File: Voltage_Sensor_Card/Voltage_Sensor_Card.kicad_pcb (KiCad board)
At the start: 2 copper layers, 59 parts, among them J1 Conn_01x04, U1 ACPL-C79B, U2 MEJ1S1205SC, U3 OPA2197xD

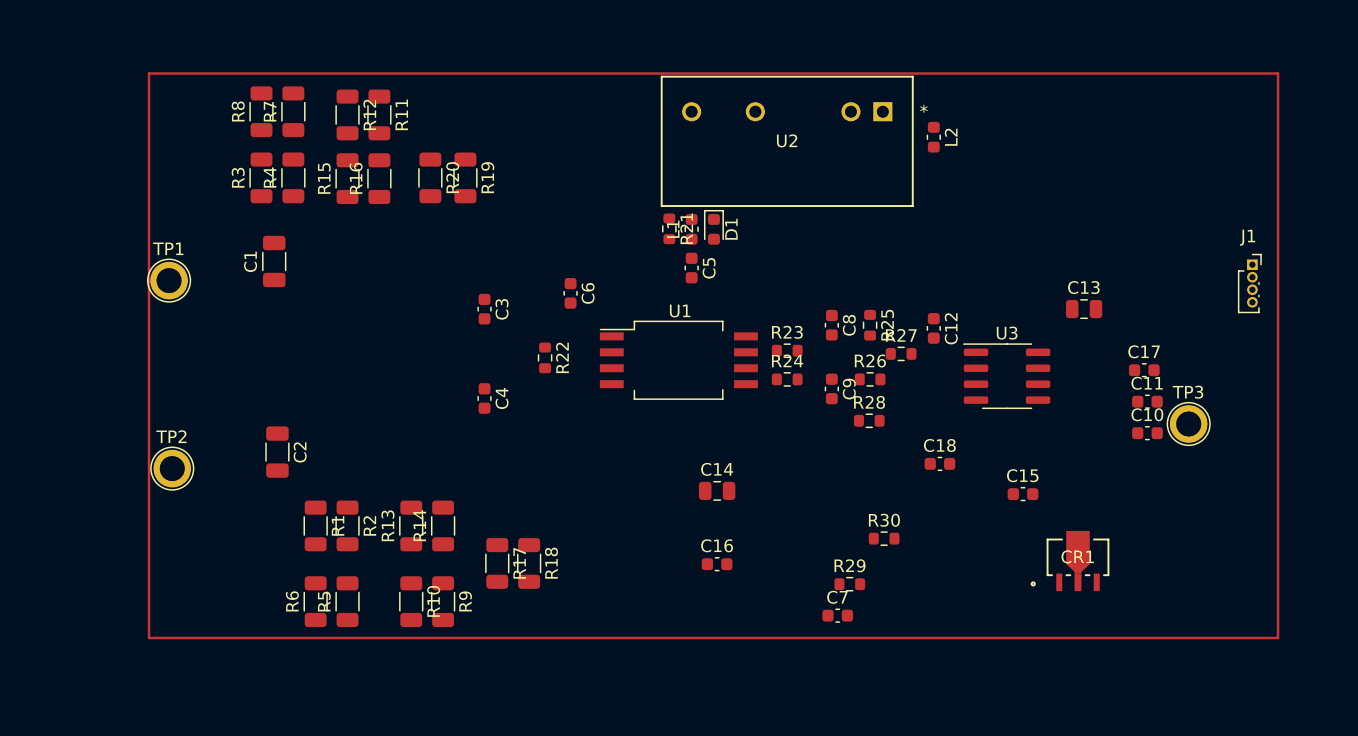
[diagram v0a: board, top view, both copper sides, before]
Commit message: Edited the layout.
Layout is not finalized yet, needs to be revised with an experienced team member.
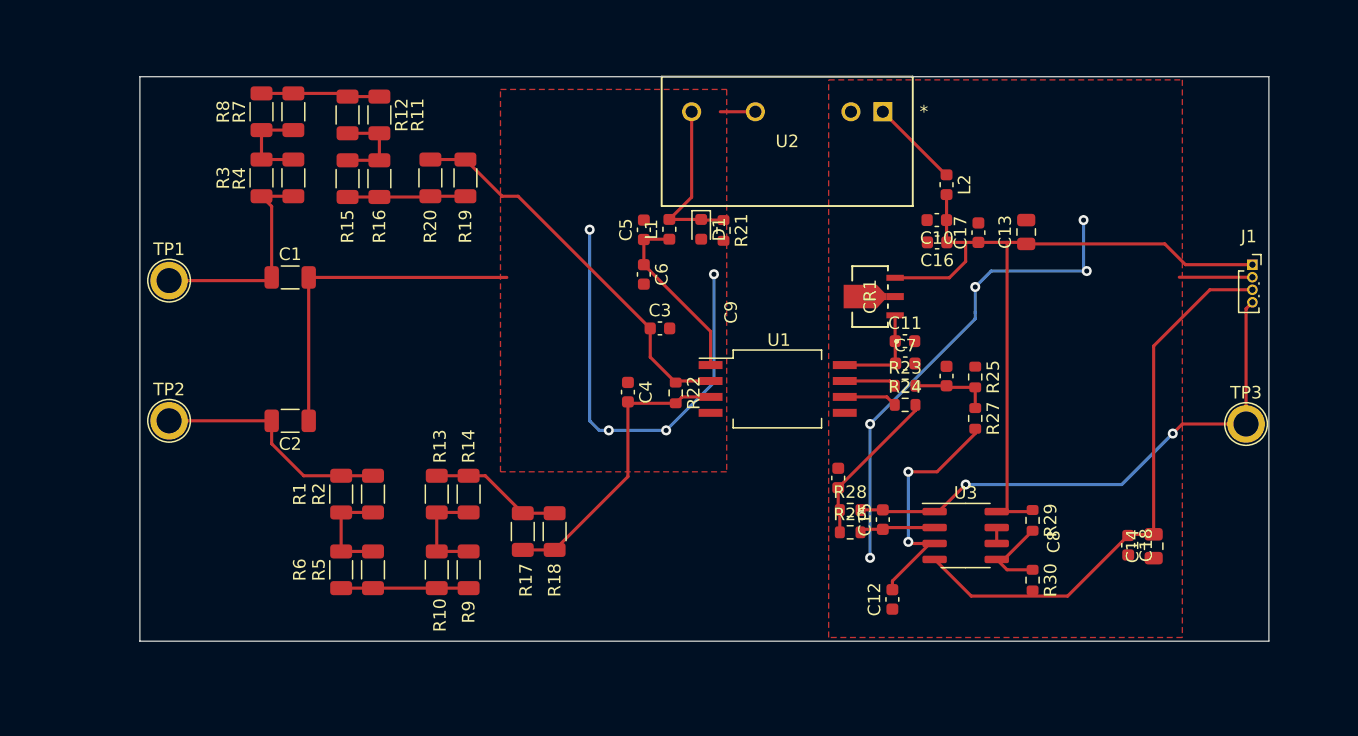
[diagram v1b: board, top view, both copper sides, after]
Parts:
- moved C14 35.1 mm to (180.1, 93.6), turned to 90 degrees
- moved C16 31.1 mm to (162.8, 69.3), turned to 180 degrees
- moved CR1 26.6 mm to (157.5, 73.7), turned to 90 degrees
- moved C10 23.9 mm to (162.8, 67.6), turned to 180 degrees
- moved C12 21.9 mm to (159.3, 97.8), turned to 90 degrees
- moved C7 20.8 mm to (160.3, 79.0)
- moved C11 19.9 mm to (160.3, 77.2)
- moved C17 17.2 mm to (166.1, 68.6), turned to 90 degrees
- moved C18 16.3 mm to (178.1, 93.5), turned to -90 degrees
- moved R29 15.4 mm to (170.4, 91.5), turned to -90 degrees
- moved C3 14.1 mm to (140.7, 76.2), turned to 0 degrees
- moved U3 13.1 mm to (165.1, 92.7)
- moved R26 12.3 mm to (155.9, 92.5)
- moved R30 12.3 mm to (170.4, 96.3), turned to -90 degrees
- moved C4 11.4 mm to (138.2, 81.3)
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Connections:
- C11 pad 1: +5V -> +5VA
- C5 pad 2: GND2 -> GND1
- CR1 pad 1: +5V -> +5VA
- D1 pad 2: GND2 -> GND1
- R21 pad 2: GND2 -> GND1
- U2 pad 5: GND2 -> GND1
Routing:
- net GND1: track 0.00 -> 65.7 mm, vias 0 -> 4
- net +15V: track 0.00 -> 60.9 mm
- net -15V: track 0.00 -> 45.5 mm
- net GND2: track 0.00 -> 44.5 mm, vias 0 -> 5
- net /Measure: track 0.00 -> 43.6 mm, vias 0 -> 2
- net Net-(C3-Pad1): track 0.00 -> 31.1 mm
- net Net-(C4-Pad2): track 0.00 -> 23.6 mm
- net Net-(C12-Pad2): track 0.00 -> 20.0 mm, vias 0 -> 2
- net Net-(C2-Pad2): track 0.00 -> 19.1 mm
- net Net-(C1-Pad1): track 0.00 -> 17.8 mm
- net +5V: track 0.00 -> 14.3 mm
- net Net-(D1-Pad1): track 0.00 -> 13.7 mm
- net Net-(C9-Pad1): track 0.00 -> 12.8 mm
- net Net-(R13-Pad2): track 0.00 -> 10.6 mm
- net Net-(R10-Pad1): track 0.00 -> 10.2 mm
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- added copper zone on F.Cu, net GND1
- added copper zone on F.Cu, net GND2
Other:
- board outline added: 90 x 45 mm

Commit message: Revized the layout.
Changed the orientation and placement of components, added all tracks and copper pours.
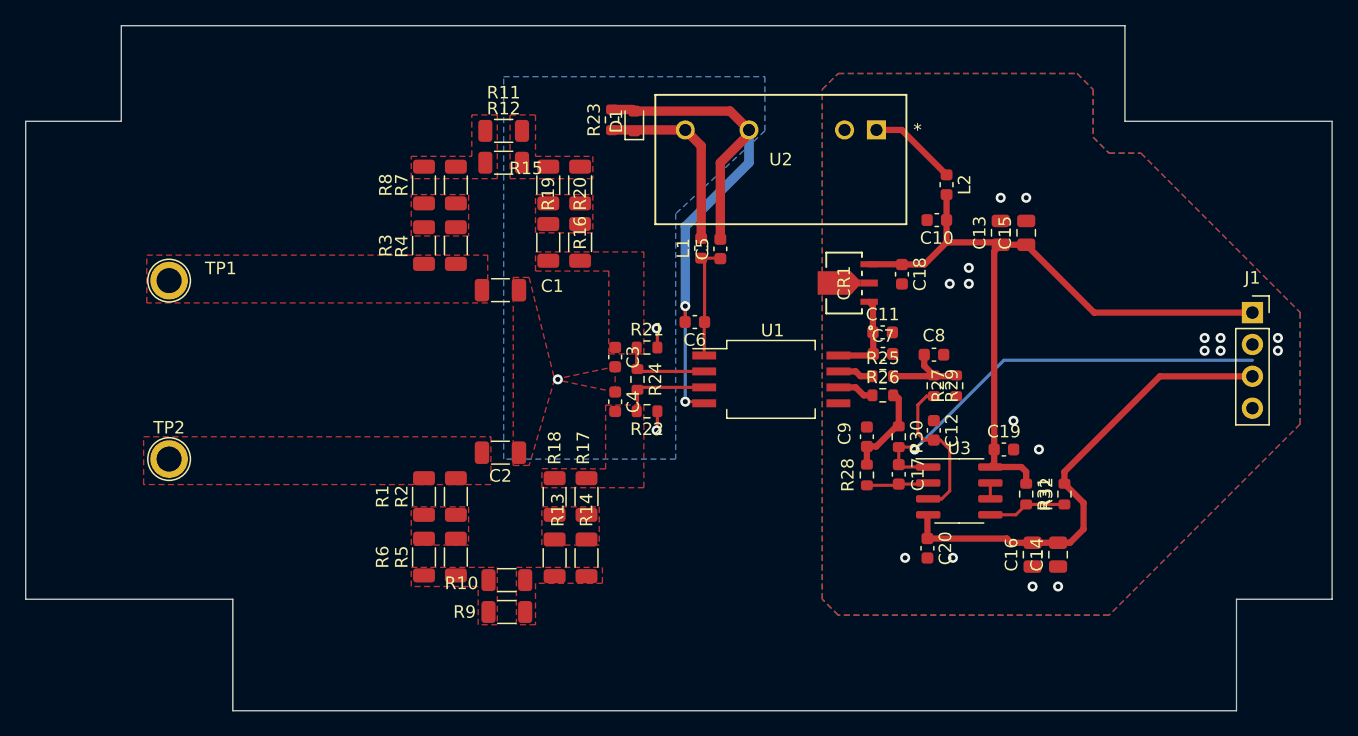
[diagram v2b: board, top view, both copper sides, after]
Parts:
- removed TP3: TestPoint, TestPoint:TestPoint_Plated_Hole_D2.0mm
- added C13: 10u, Capacitor_SMD:C_0805_2012Metric, F.Cu at (167.9, 68.6)
- added C14: 10u, Capacitor_SMD:C_0805_2012Metric, F.Cu at (172.5, 94.2)
- added R21: 10k, Resistor_SMD:R_0603_1608Metric, F.Cu at (139.7, 77.7)
- added R22: 10k, Resistor_SMD:R_0603_1608Metric, F.Cu at (139.7, 82.8)
- J1: footprint Connector_PinSocket_1.00mm:PinSocket_1x04_P1.00mm_Vertical -> Connector_PinSocket_2.54mm:PinSocket_1x04_P2.54mm_Vertical
- moved C19 17.4 mm to (168.1, 85.9), turned to 0 degrees
- moved C2 17.0 mm to (128.0, 86.1)
- moved C1 16.8 mm to (128.0, 73.2)
- moved R16 16.0 mm to (134.4, 64.8)
- moved R15 16.0 mm to (131.8, 64.8)
- moved C20 16.0 mm to (162.1, 93.7)
- moved R8 14.2 mm to (121.9, 64.8)
- moved R7 14.2 mm to (124.5, 64.8)
- moved R3 14.0 mm to (121.9, 69.6)
- moved R4 14.0 mm to (124.5, 69.6)
- moved C12 13.9 mm to (162.6, 84.3), turned to -90 degrees
- moved R12 13.0 mm to (128.3, 63.0), turned to 0 degrees
- moved R20 13.0 mm to (134.4, 69.3), turned to -90 degrees
- moved R23 12.5 mm to (136.9, 59.6), turned to 90 degrees
- moved R13 10.7 mm to (132.3, 94.5)
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- renumbered C13 to C15, C14 to C16, C15 to C17, C16 to C18, C17 to C19, C18 to C20, R21 to R23, R22 to R24, R23 to R25, R24 to R26, R25 to R27, R26 to R28, R27 to R29, R28 to R30, R29 to R31, R30 to R32
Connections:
- net Net-(C1-Pad1) renamed /Input +
- net Net-(C2-Pad2) renamed /Input -
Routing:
- net GND2: track 44.5 -> 0.00 mm, vias 5 -> 17
- net Net-(C3-Pad1): track 31.1 -> 7.14 mm
- net /Input -: track 19.1 -> 0.00 mm
- net /Input +: track 17.8 -> 0.00 mm
- net Net-(C4-Pad2): track 23.6 -> 7.14 mm
- net GND1: track 65.7 -> 51.0 mm, vias 4 -> 5
- net Net-(R13-Pad2): track 10.6 -> 0.00 mm
- net Net-(R10-Pad1): track 10.2 -> 0.00 mm
- net Net-(R15-Pad2): track 9.87 -> 0.00 mm
- net Net-(R11-Pad1): track 9.50 -> 0.00 mm
- net /Measure: track 43.6 -> 35.0 mm, vias 2 -> 1
- net Net-(R10-Pad2): track 8.19 -> 0.00 mm
- net Net-(R1-Pad2): track 8.19 -> 0.00 mm
- net Net-(C12-Pad2): track 20.0 -> 12.2 mm, vias 2 -> 0
- net Net-(R3-Pad2): track 7.43 -> 0.00 mm
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- added copper zone on F.Cu, net /Input +
- added copper zone on F.Cu, net /Input -
- added copper zone on B.Cu, net GND1
- added copper zone on B.Cu, net GND2
- added copper zone on F.Cu, net Net-(C3-Pad1)
- added copper zone on F.Cu, net Net-(C4-Pad2)
- added copper zone on F.Cu, net Net-(R1-Pad2)
- added copper zone on F.Cu, net Net-(R10-Pad1)
- added copper zone on F.Cu, net Net-(R10-Pad2)
- added copper zone on F.Cu, net Net-(R11-Pad1)
- added copper zone on F.Cu, net Net-(R11-Pad2)
- added copper zone on F.Cu, net Net-(R13-Pad2)
- added copper zone on F.Cu, net Net-(R15-Pad2)
- added copper zone on F.Cu, net Net-(R3-Pad2)
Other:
- board size 90 x 45 mm -> 104.1 x 54.6 mm
- board text added: "08.01.08"
- board text added: "1"
- board text added: "2"
- board text added: "3"
- board text added: "4"
- board text added: "5"
- board text added: "6"
- board text added: "A"
- board text added: "A4"
- board text added: "ABS Enclosure"
- board text added: "ANY REPRODUCTION IN PART OR AS A WHOLE"
- board text added: "ARTICLE NO:"
- board text added: "B"
- board text added: "C"
- board text added: "CHECKED"
- board text added: "COMMENTS:"
- board text added: "D"
- board text added: "DATE"
- board text added: "DEBUR AND BREAK SHARP EDGES"
- board text added: "DIMENSIONS ARE IN MILLIMETERS,"
- board text added: "DRAWN"
- board text added: "DWG NO."
- board text added: "ENCLOSURES FOR ELECTRONICS"
- board text added: "ENCLOSURES IS PROHIBITED."
- board text added: "MATERIAL:"
- board text added: "NAME"
- board text added: "PROPRIETARY AND CONFIDENTIAL"
- board text added: "REVISION:"
- board text added: "SCALE:1:1"
- board text added: "SE-210 IP-65 Dark Gray"
- board text added: "SE-210-0-0-D-0-10765"
- board text added: "SHEET 1 OF 1"
- board text added: "THE INFORMATION CONTAINED IN THIS DRAWING IS"
- board text added: "THE SOLE PROPERTY OF ALTINKAYA ENCLOSURES."
- board text added: "TITLE:"
- board text added: "WEIGHT:"
- board text added: "WITHOUT THE WRITTEN PERMISSION OF ALTINKAYA"
- board text added: "www.altinkaya.com.tr"
